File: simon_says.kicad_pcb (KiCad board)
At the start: 2 copper layers, 97 x 60 mm, 22 parts, among them SW1 SW_Push_LED, SW2 SW_Push_LED, SW3 SW_Push_LED, SW4 SW_Push_LED, U1 ATtiny25-20P

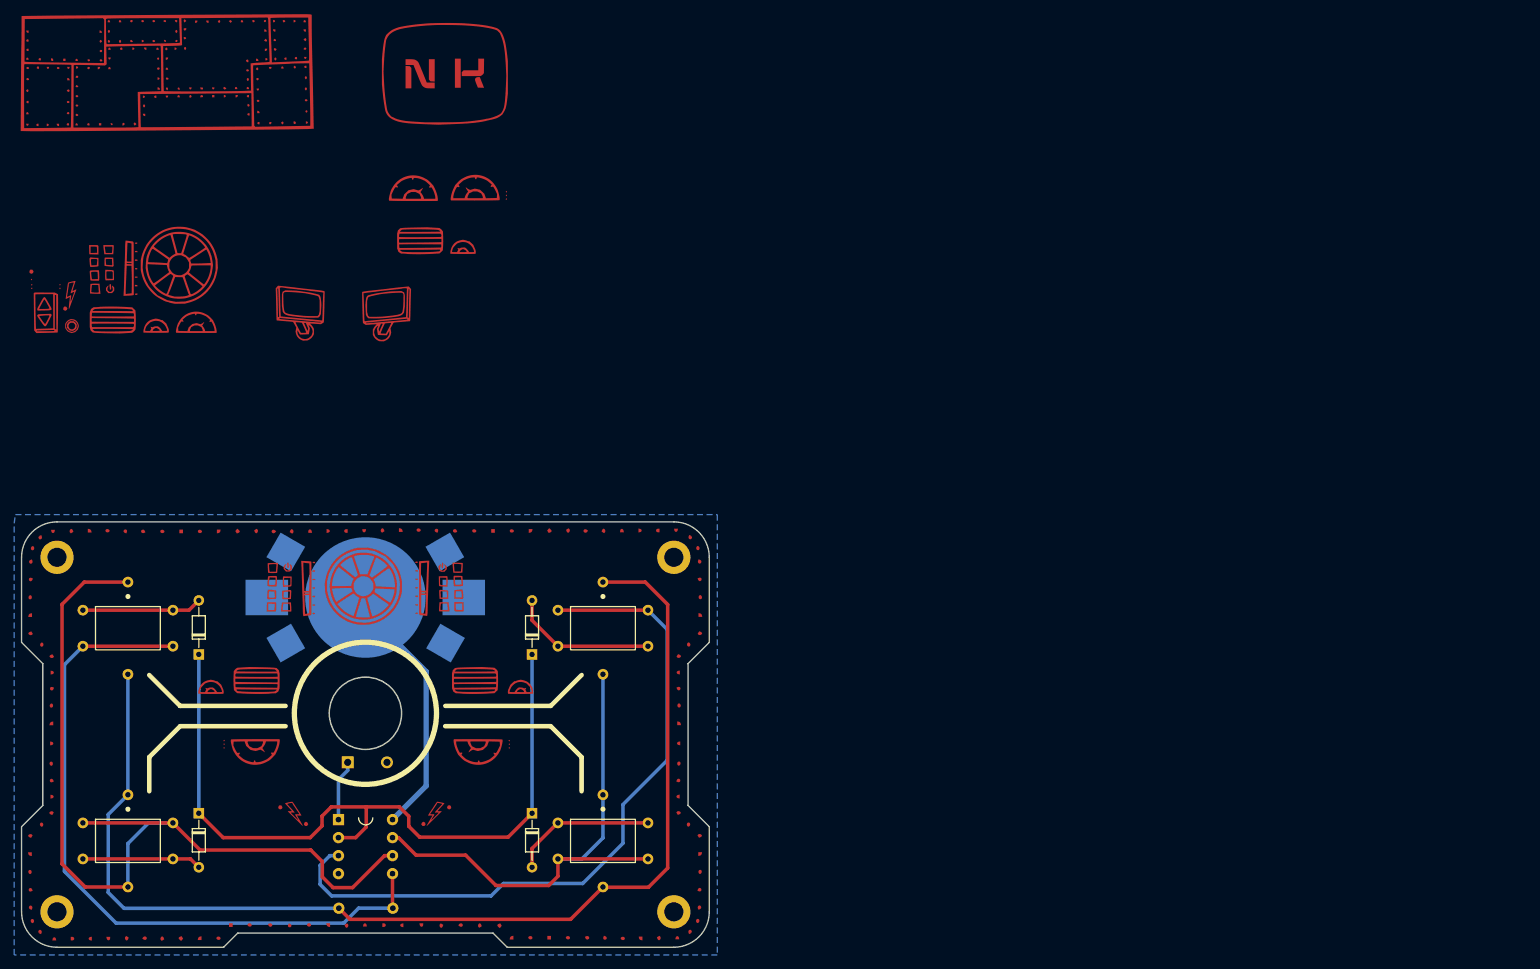
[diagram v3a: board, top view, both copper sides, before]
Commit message: The great remake! - added decoupling capacitor - replaced speaker with piezo - added 2450 cell holder - added extra button - rerouted all traces
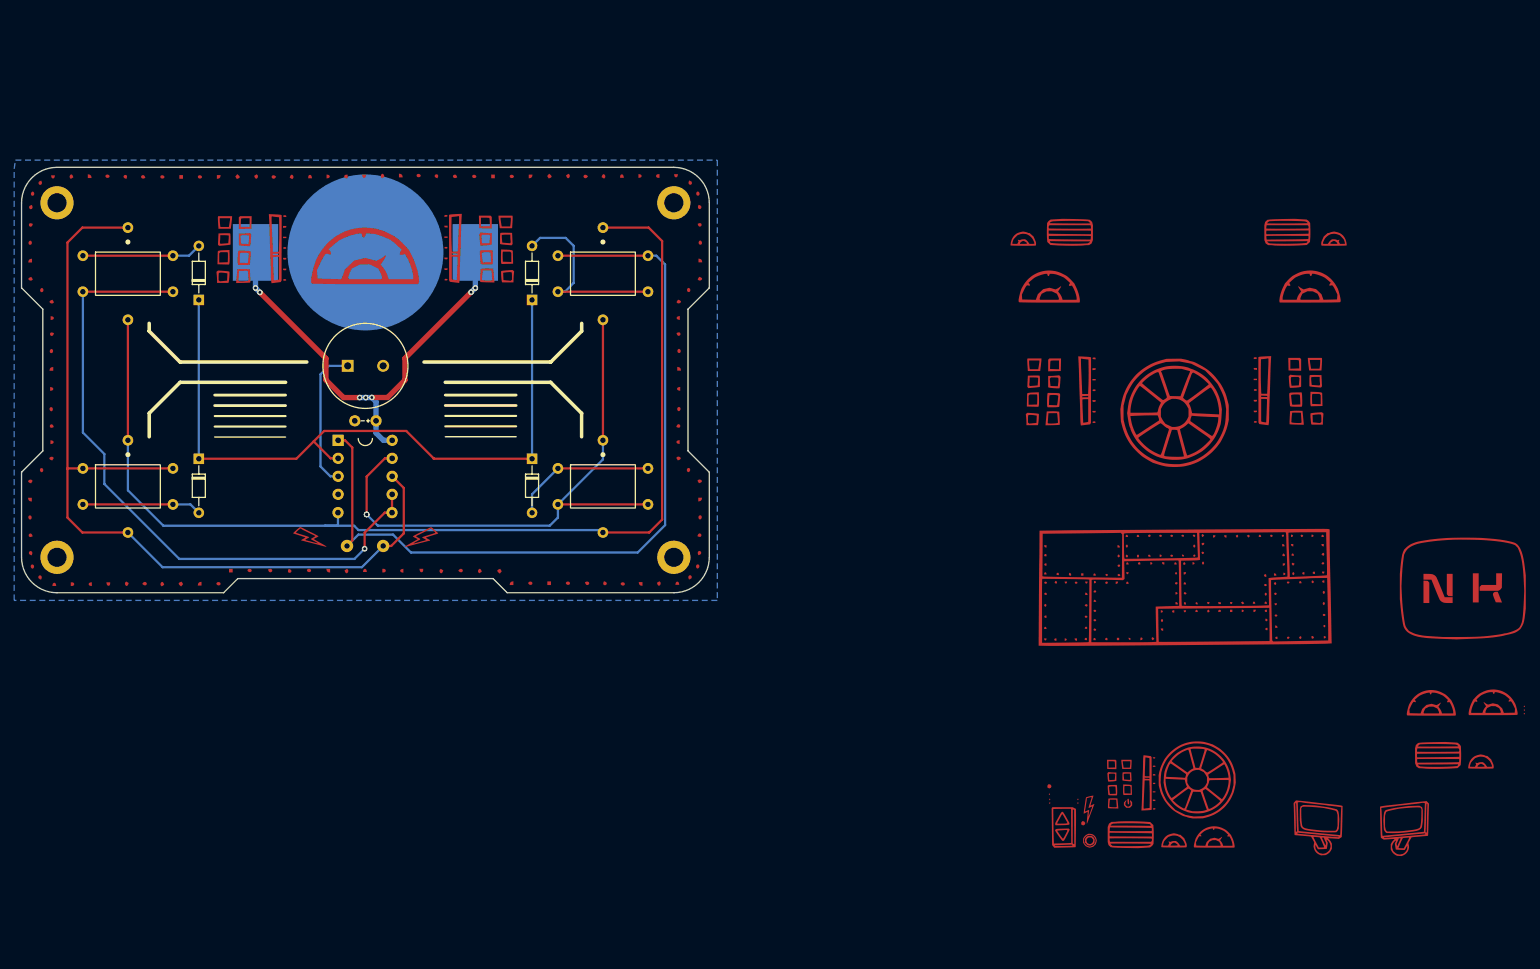
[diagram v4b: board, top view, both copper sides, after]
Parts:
- removed the ? at (88.8, 104.3)
- removed the ? at (87.4, 117.1)
- removed the ? at (85.6, 110.7)
- removed the ? at (111.4, 104.3)
- removed the REF** at (111.9, 110.7)
- removed the REF** at (109.7, 117.1)
- added ?: , , F.Cu at (114.0, 62.0)
- added ?: , , F.Cu at (83.0, 62.0)
- added C1: C, Capacitor_THT:CP_Radial_Tantal_D4.5mm_P2.50mm, F.Cu at (98.5, 85.8)
- added SW5: SW_Push, Button_Switch_SMD:SW_MEC_5GSH9, F.Cu at (98.5, 103.4)
- moved LS1 55.9 mm to (98.5, 78.0), turned to 0 degrees
- moved R1 55.8 mm to (102.2, 98.7)
- moved U1 53.5 mm to (94.7, 88.5)
- moved D1 50.0 mm to (75.0, 68.7)
- moved D2 50.0 mm to (75.0, 91.1)
- moved D3 50.0 mm to (122.0, 91.1)
- moved D4 50.0 mm to (122.0, 68.7)
- moved REF** 50.0 mm to (55.0, 55.0)
- moved REF** 50.0 mm to (142.0, 105.0)
- moved REF** 50.0 mm to (142.0, 55.0)
- moved REF** 50.0 mm to (55.0, 105.0)
- moved SW1 50.0 mm to (65.0, 65.0)
- moved SW2 50.0 mm to (65.0, 95.0)
- moved SW3 50.0 mm to (132.0, 95.0)
- moved SW4 50.0 mm to (132.0, 65.0)
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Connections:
- REF** pad 1: +BATT -> -BATT
- U1 pad 1: SPK -> MM4
- U1 pad 3: MM4 -> SPK
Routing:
- net +BATT: track 36.8 -> 71.0 mm, vias 0 -> 7
- net MM4: track 101.7 -> 117.2 mm
- net SPK: track 8.62 -> 20.4 mm
- net MM3: track 72.5 -> 81.4 mm, vias 0 -> 2
- net Net-(SW1-A): track 163.1 -> 154.7 mm
- net MM1: track 100.7 -> 92.6 mm, vias 0 -> 1
- net BTNS: track 107.2 -> 99.6 mm
- net Net-(D4-A): track 20.9 -> 27.5 mm
- net MM2: track 122.1 -> 124.1 mm
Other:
- outline, holes or cut-outs redrawn
